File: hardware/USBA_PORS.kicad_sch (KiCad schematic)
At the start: 29 parts, among them J3 0483930003, J4 0483930003, J5 0483930003, J6 0483930003

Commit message: finaliseing pcb layout will come back later for a fresh look
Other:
- company: (none) -> MICK MAKE
- title: (none) -> 200W USB PD 3.1 HUB
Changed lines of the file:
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@@
 (kicad_sch (version 20230121) (generator eeschema)
   (paper "A4")
+  (title_block
+    (title "200W USB PD 3.1 HUB")
+    (date "2023-10-03")
+    (rev "A")
+    (company "MICK MAKE")
+    (comment 1 "THIS IS A 2X 100W USB PD SOURCE ")
+    (comment 2 "HUB USB SPEC 3.1")
+    (comment 3 "TOTAL SYSTEM POWER IS ~275w")
+  )
   (junction (at 93.98 127) (diameter 0) (color 0 0 0 0)
   )

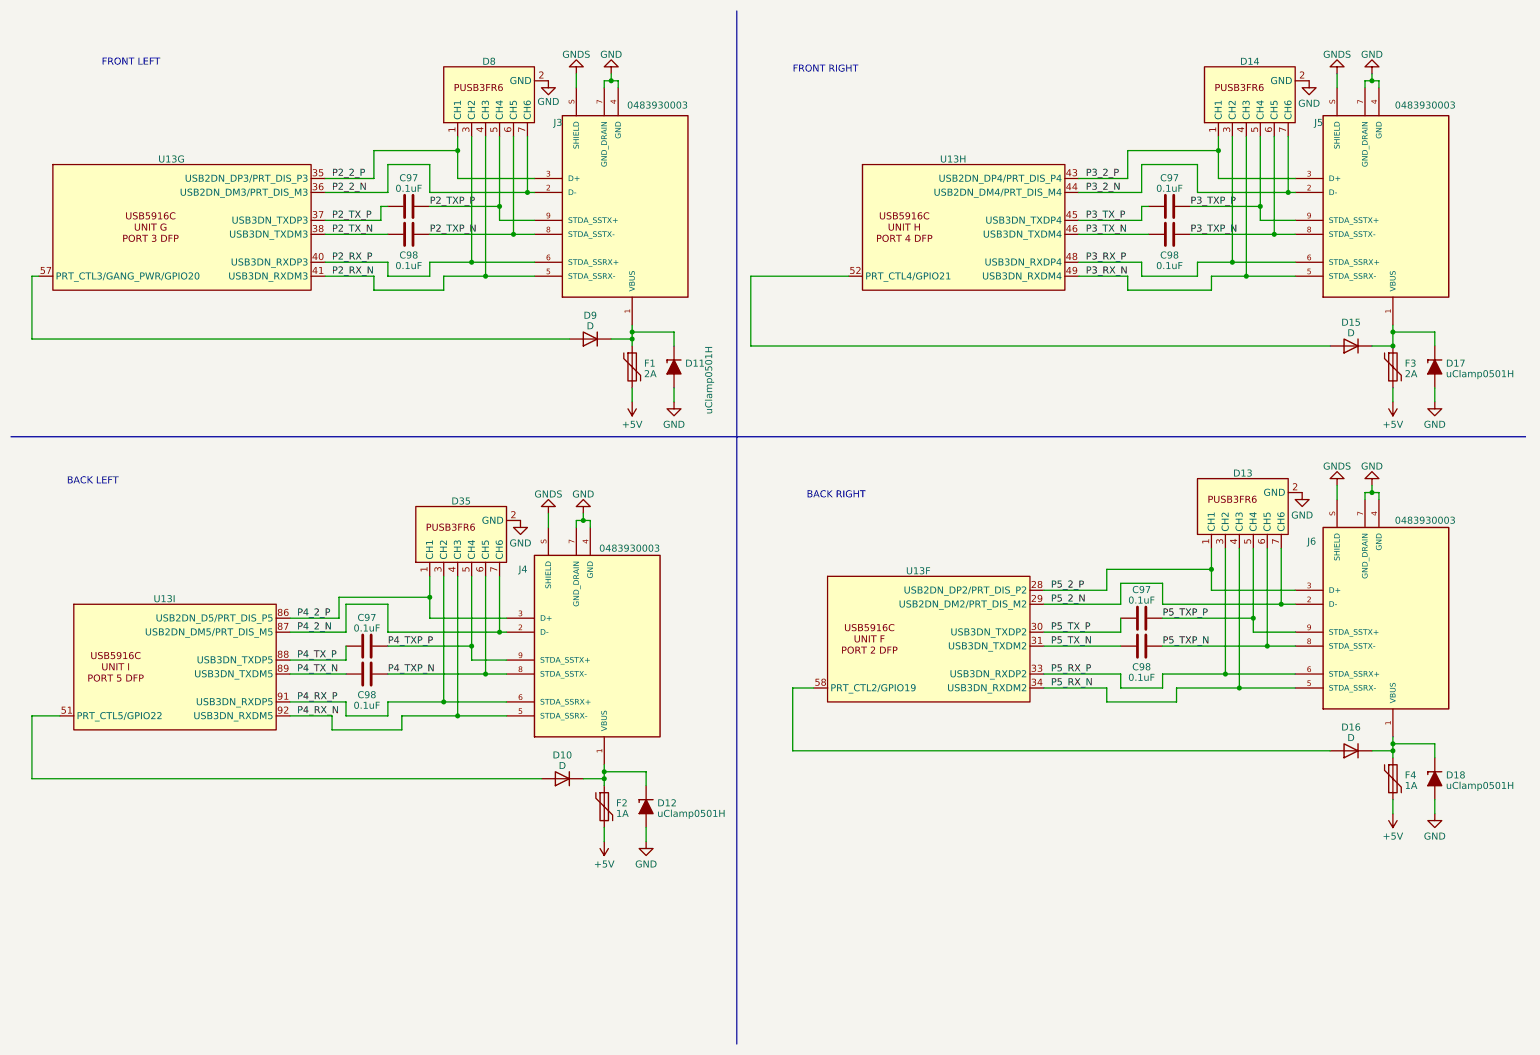
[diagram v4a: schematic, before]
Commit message: working on fixing pcb impeedance
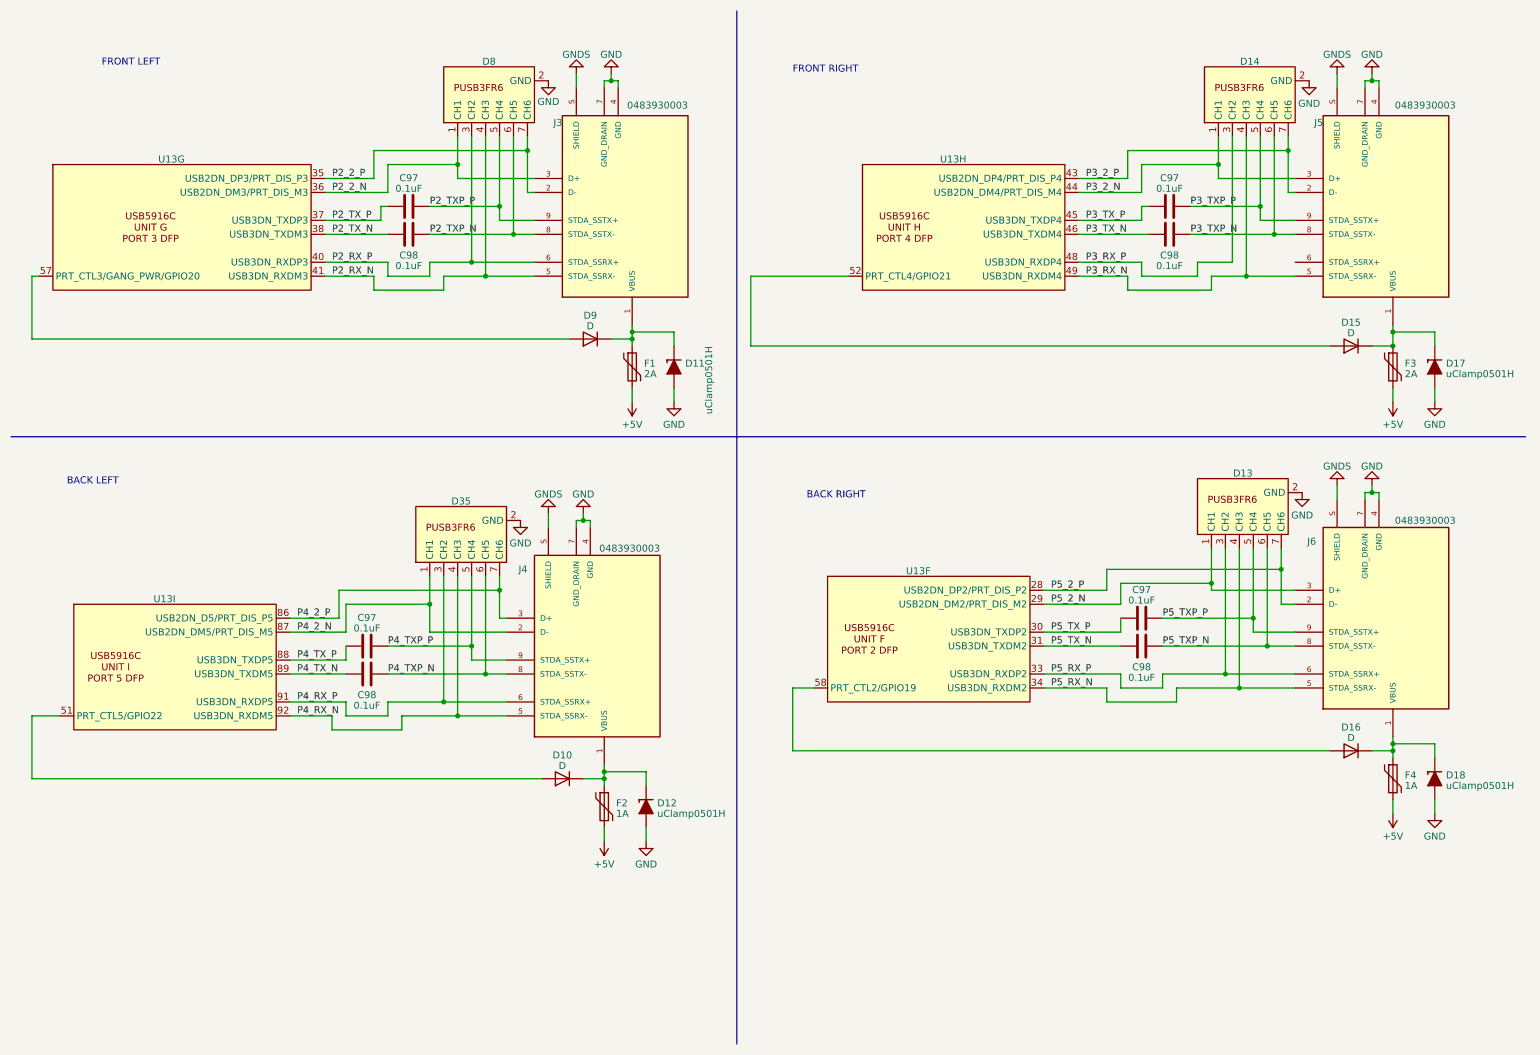
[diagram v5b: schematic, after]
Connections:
- net P2_2_N: now also D8.1 (CH1), J3.3 (D+); no longer D8.7 (CH6), J3.2 (D-)
- net P2_2_P: now also D8.7 (CH6), J3.2 (D-); no longer D8.1 (CH1), J3.3 (D+)
- net P3_2_N: now also D14.1 (CH1), J5.3 (D+); no longer D14.7 (CH6), J5.2 (D-)
- net P3_2_P: now also D14.7 (CH6), J5.2 (D-); no longer D14.1 (CH1), J5.3 (D+)
- net P3_RX_P: no longer J5.6 (STDA_SSRX+)
- net P4_2_N: now also D35.1 (CH1); no longer D35.7 (CH6)
- net P4_2_P: now also D35.7 (CH6); no longer D35.1 (CH1)
- net P5_2_N: now also D13.1 (CH1), J6.3 (D+); no longer D13.7 (CH6), J6.2 (D-)
- net P5_2_P: now also D13.7 (CH6), J6.2 (D-); no longer D13.1 (CH1), J6.3 (D+)

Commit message: fixed DP issues and finneshed overall routeing
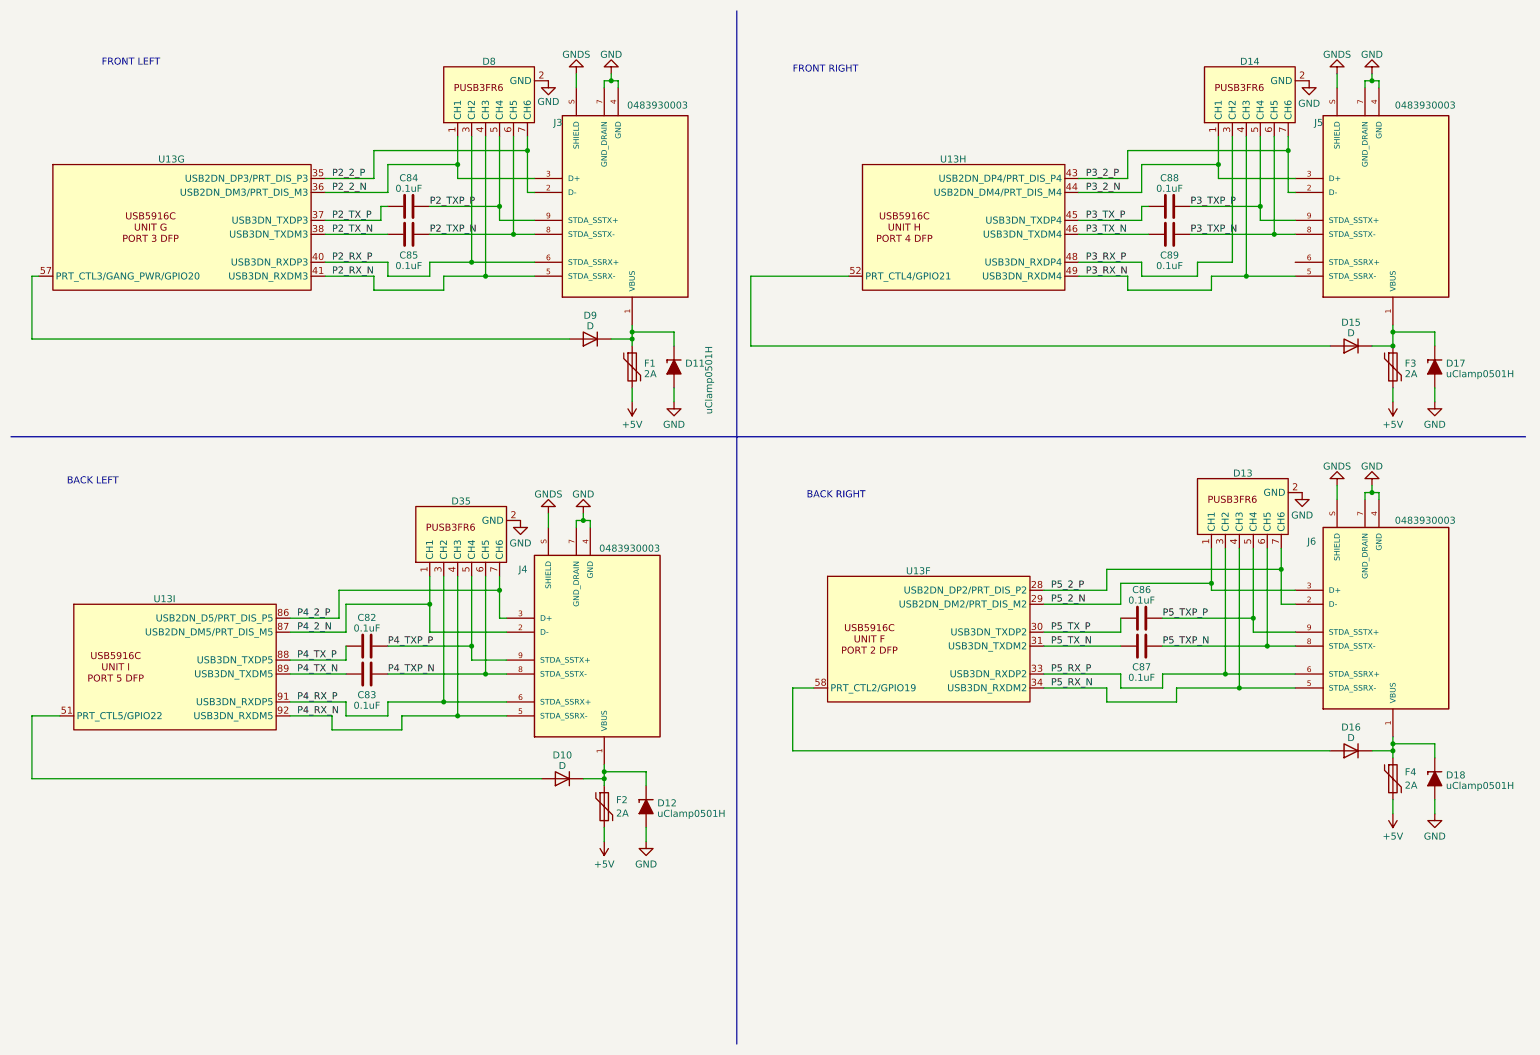
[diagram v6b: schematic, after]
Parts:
- F2, F4: value 1A -> 2A
- renumbered C97 to C82, C98 to C83, C97 to C84, C98 to C85, C97 to C86, C98 to C87, C97 to C88, C98 to C89
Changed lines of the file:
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@@
   (symbol (lib_id "Device:C") (at 74.93 132.08 270) (unit 1)
     (in_bom yes) (on_board yes) (dnp no)
-    (property "Reference" "C98" (at 74.93 135.89 90)
+    (property "Reference" "C83" (at 74.93 135.89 90)
       (effects (font (size 1.27 1.27)))
     )
@@
     (instances
       (project "usbc-car-module"
-        (path "/fae025e9-99c5-40c1-af6f-99dc1edbfa43/bb20a659-2b02-48fa-8ef7-389a14e86ba7"
-          (reference "C98") (unit 1)
-        )
         (path "/fae025e9-99c5-40c1-af6f-99dc1edbfa43/fe8e7353-13b3-4aa6-97f7-d88e32d23b04"
           (reference "C83") (unit 1)
@@
   (symbol (lib_id "Device:Polyfuse") (at 118.11 156.21 0) (unit 1)
     (in_bom yes) (on_board yes) (dnp no) (fields_autoplaced)
-    (property "Reference" "F2" (at 120.269 155.5663 0)
+    (property "Reference" "F2" (at 120.269 154.9979 0)
       (effects (font (size 1.27 1.27)) (justify left))
     )
-    (property "Value" "1A" (at 120.269 157.4873 0)
+    (property "Value" "2A" (at 120.269 157.4221 0)
       (effects (font (size 1.27 1.27)) (justify left))
     )
@@
   (symbol (lib_id "Device:C") (at 220.98 46.99 90) (unit 1)
     (in_bom yes) (on_board yes) (dnp no) (fields_autoplaced)
-    (property "Reference" "C97" (at 220.98 41.8211 90)
+    (property "Reference" "C88" (at 220.98 41.8211 90)
       (effects (font (size 1.27 1.27)))
     )
@@
     (instances
       (project "usbc-car-module"
-        (path "/fae025e9-99c5-40c1-af6f-99dc1edbfa43/bb20a659-2b02-48fa-8ef7-389a14e86ba7"
-          (reference "C97") (unit 1)
-        )
         (path "/fae025e9-99c5-40c1-af6f-99dc1edbfa43/fe8e7353-13b3-4aa6-97f7-d88e32d23b04"
           (reference "C88") (unit 1)
@@
           (reference "U13") (unit 7)
         )
-        (path "/fae025e9-99c5-40c1-af6f-99dc1edbfa43/7a7a6512-c96f-448a-bb8d-4d6e185adf7f"
-          (reference "U13") (unit 7)
-        )
       )
     )
@@
           (reference "U13") (unit 6)
         )
-        (path "/fae025e9-99c5-40c1-af6f-99dc1edbfa43/7a7a6512-c96f-448a-bb8d-4d6e185adf7f"
-          (reference "U13") (unit 6)
-        )
       )
     )
@@
   (symbol (lib_id "Device:C") (at 82.55 46.99 90) (unit 1)
     (in_bom yes) (on_board yes) (dnp no) (fields_autoplaced)
-    (property "Reference" "C97" (at 82.55 41.8211 90)
+    (property "Reference" "C84" (at 82.55 41.8211 90)
       (effects (font (size 1.27 1.27)))
     )
@@
     (instances
       (project "usbc-car-module"
-        (path "/fae025e9-99c5-40c1-af6f-99dc1edbfa43/bb20a659-2b02-48fa-8ef7-389a14e86ba7"
-          (reference "C97") (unit 1)
-        )
         (path "/fae025e9-99c5-40c1-af6f-99dc1edbfa43/fe8e7353-13b3-4aa6-97f7-d88e32d23b04"
           (reference "C84") (unit 1)
@@
   (symbol (lib_id "Device:C") (at 215.9 127 270) (unit 1)
     (in_bom yes) (on_board yes) (dnp no)
-    (property "Reference" "C98" (at 215.9 130.81 90)
+    (property "Reference" "C87" (at 215.9 130.81 90)
       (effects (font (size 1.27 1.27)))
     )
@@
     (instances
       (project "usbc-car-module"
-        (path "/fae025e9-99c5-40c1-af6f-99dc1edbfa43/bb20a659-2b02-48fa-8ef7-389a14e86ba7"
-          (reference "C98") (unit 1)
-        )
         (path "/fae025e9-99c5-40c1-af6f-99dc1edbfa43/fe8e7353-13b3-4aa6-97f7-d88e32d23b04"
           (reference "C87") (unit 1)
@@
           (reference "U13") (unit 9)
         )
-        (path "/fae025e9-99c5-40c1-af6f-99dc1edbfa43/7a7a6512-c96f-448a-bb8d-4d6e185adf7f"
-          (reference "U13") (unit 9)
-        )
       )
     )
@@
           (reference "U13") (unit 8)
         )
-        (path "/fae025e9-99c5-40c1-af6f-99dc1edbfa43/7a7a6512-c96f-448a-bb8d-4d6e185adf7f"
-          (reference "U13") (unit 8)
-        )
       )
     )
@@
   (symbol (lib_id "Device:C") (at 220.98 52.07 270) (unit 1)
     (in_bom yes) (on_board yes) (dnp no)
-    (property "Reference" "C98" (at 220.98 55.88 90)
+    (property "Reference" "C89" (at 220.98 55.88 90)
       (effects (font (size 1.27 1.27)))
     )
@@
     (instances
       (project "usbc-car-module"
-        (path "/fae025e9-99c5-40c1-af6f-99dc1edbfa43/bb20a659-2b02-48fa-8ef7-389a14e86ba7"
-          (reference "C98") (unit 1)
-        )
         (path "/fae025e9-99c5-40c1-af6f-99dc1edbfa43/fe8e7353-13b3-4aa6-97f7-d88e32d23b04"
           (reference "C89") (unit 1)
@@
   (symbol (lib_id "Device:C") (at 215.9 121.92 90) (unit 1)
     (in_bom yes) (on_board yes) (dnp no) (fields_autoplaced)
-    (property "Reference" "C97" (at 215.9 116.7511 90)
+    (property "Reference" "C86" (at 215.9 116.7511 90)
       (effects (font (size 1.27 1.27)))
     )
@@
     (instances
       (project "usbc-car-module"
-        (path "/fae025e9-99c5-40c1-af6f-99dc1edbfa43/bb20a659-2b02-48fa-8ef7-389a14e86ba7"
-          (reference "C97") (unit 1)
-        )
         (path "/fae025e9-99c5-40c1-af6f-99dc1edbfa43/fe8e7353-13b3-4aa6-97f7-d88e32d23b04"
           (reference "C86") (unit 1)
@@
   (symbol (lib_id "Device:C") (at 74.93 127 90) (unit 1)
     (in_bom yes) (on_board yes) (dnp no) (fields_autoplaced)
-    (property "Reference" "C97" (at 74.93 121.8311 90)
+    (property "Reference" "C82" (at 74.93 121.8311 90)
       (effects (font (size 1.27 1.27)))
     )
@@
     (instances
       (project "usbc-car-module"
-        (path "/fae025e9-99c5-40c1-af6f-99dc1edbfa43/bb20a659-2b02-48fa-8ef7-389a14e86ba7"
-          (reference "C97") (unit 1)
-        )
         (path "/fae025e9-99c5-40c1-af6f-99dc1edbfa43/fe8e7353-13b3-4aa6-97f7-d88e32d23b04"
           (reference "C82") (unit 1)
@@
   (symbol (lib_id "Device:C") (at 82.55 52.07 270) (unit 1)
     (in_bom yes) (on_board yes) (dnp no)
-    (property "Reference" "C98" (at 82.55 55.88 90)
+    (property "Reference" "C85" (at 82.55 55.88 90)
       (effects (font (size 1.27 1.27)))
     )
@@
     (instances
       (project "usbc-car-module"
-        (path "/fae025e9-99c5-40c1-af6f-99dc1edbfa43/bb20a659-2b02-48fa-8ef7-389a14e86ba7"
-          (reference "C98") (unit 1)
-        )
         (path "/fae025e9-99c5-40c1-af6f-99dc1edbfa43/fe8e7353-13b3-4aa6-97f7-d88e32d23b04"
           (reference "C85") (unit 1)
@@
   (symbol (lib_id "Device:Polyfuse") (at 261.62 151.13 0) (unit 1)
     (in_bom yes) (on_board yes) (dnp no) (fields_autoplaced)
-    (property "Reference" "F4" (at 263.779 150.4863 0)
+    (property "Reference" "F4" (at 263.779 149.9179 0)
       (effects (font (size 1.27 1.27)) (justify left))
     )
-    (property "Value" "1A" (at 263.779 152.4073 0)
+    (property "Value" "2A" (at 263.779 152.3421 0)
       (effects (font (size 1.27 1.27)) (justify left))
     )

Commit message: minor revisions
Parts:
- D13, D14, D35, D8: value ~ -> PUSB3AB6Z
- U13: value ~ -> USB5926C
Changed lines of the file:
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@@
   )
   (symbol (lib_id "CARTHING:PUSB3FR6") (at 233.68 101.6 90) (unit 1)
-    (in_bom yes) (on_board yes) (dnp no) (fields_autoplaced)
+    (in_bom yes) (on_board yes) (dnp no)
     (property "Reference" "D13" (at 234.315 95.5581 90)
       (effects (font (size 1.27 1.27)))
     )
-    (property "Value" "~" (at 215.9 107.95 0)
+    (property "Value" "PUSB3AB6Z" (at 224.79 102.87 0)
       (effects (font (size 1.27 1.27)))
     )
@@
       (effects (font (size 1.27 1.27)))
     )
-    (property "Value" "~" (at 33.02 19.05 0)
+    (property "Value" "USB5926C" (at 59.69 38.1 0)
       (effects (font (size 1.27 1.27)))
     )
@@
       (effects (font (size 1.27 1.27)))
     )
-    (property "Value" "~" (at 168.91 93.98 0)
+    (property "Value" "USB5926C" (at 190.5 113.03 0)
       (effects (font (size 1.27 1.27)))
     )
@@
   )
   (symbol (lib_id "CARTHING:PUSB3FR6") (at 96.52 26.67 90) (unit 1)
-    (in_bom yes) (on_board yes) (dnp no) (fields_autoplaced)
+    (in_bom yes) (on_board yes) (dnp no)
     (property "Reference" "D8" (at 97.155 20.6281 90)
       (effects (font (size 1.27 1.27)))
     )
-    (property "Value" "~" (at 78.74 33.02 0)
+    (property "Value" "PUSB3AB6Z" (at 86.36 26.67 0)
       (effects (font (size 1.27 1.27)))
     )
@@
   )
   (symbol (lib_id "CARTHING:PUSB3FR6") (at 91.44 106.68 90) (unit 1)
-    (in_bom yes) (on_board yes) (dnp no) (fields_autoplaced)
+    (in_bom yes) (on_board yes) (dnp no)
     (property "Reference" "D35" (at 92.075 100.6381 90)
       (effects (font (size 1.27 1.27)))
     )
-    (property "Value" "~" (at 73.66 113.03 0)
+    (property "Value" "PUSB3AB6Z" (at 82.55 107.95 0)
       (effects (font (size 1.27 1.27)))
     )
@@
       (effects (font (size 1.27 1.27)))
     )
-    (property "Value" "~" (at 31.75 99.06 0)
+    (property "Value" "USB5926C" (at 53.34 118.11 0)
       (effects (font (size 1.27 1.27)))
     )
@@
       (effects (font (size 1.27 1.27)))
     )
-    (property "Value" "~" (at 175.26 19.05 0)
+    (property "Value" "USB5926C" (at 196.85 38.1 0)
       (effects (font (size 1.27 1.27)))
     )
@@
   )
   (symbol (lib_id "CARTHING:PUSB3FR6") (at 234.95 26.67 90) (unit 1)
-    (in_bom yes) (on_board yes) (dnp no) (fields_autoplaced)
+    (in_bom yes) (on_board yes) (dnp no)
     (property "Reference" "D14" (at 235.585 20.6281 90)
       (effects (font (size 1.27 1.27)))
     )
-    (property "Value" "~" (at 217.17 33.02 0)
-      (effects (font (size 1.27 1.27)))
-    )
+    (property "Value" "PUSB3AB6Z" (at 224.79 26.67 0)
+      (effects (font (size 1.27 1.27)))
+    )
